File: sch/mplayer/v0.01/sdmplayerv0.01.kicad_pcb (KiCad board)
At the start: 2 copper layers, 47.2 x 69.6 mm, 73 parts, among them CON1 SD_Card, IC1 AT24CS64-SSHM, J1 JACK_TRS_6PINS, P1 USB_OTG, P2 CONN_01X09, P3 ClockBat, P4 USART1, P6 LiPo battery, SW1 SW_PUSH, SW2 Switch_SPDT_x2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

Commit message: Fixed traces
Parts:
- moved P2 19.0 mm to (187.3, 132.0)
- moved SW2 16.6 mm to (188.0, 112.3)
- moved C12 10.2 mm to (187.9, 108.3)
- moved C9 10.2 mm to (187.9, 106.0)
- moved L1 10.2 mm to (188.0, 101.7)
- moved U2 10.2 mm to (183.5, 104.0)
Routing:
- net +3V3: track 275.4 -> 321.4 mm
- net /I2C2_SDA: track 44.3 -> 16.0 mm
- net /I2C2_SCL: track 43.6 -> 15.6 mm
- net /PB2: track 42.5 -> 15.2 mm
- net /PB1: track 40.7 -> 14.8 mm
- net /PB0: track 40.2 -> 15.2 mm
- net Net-(P6-Pad2): track 7.08 -> 27.9 mm
- net /PC4: track 36.5 -> 16.0 mm
- net /PC5: track 35.9 -> 15.6 mm
- net +BATT: track 85.5 -> 104.1 mm
- net /SD_CONN: track 53.7 -> 41.5 mm
- net GND: track 537.5 -> 528.3 mm, vias 15 -> 18
- net /SD_CLK: track 53.8 -> 48.7 mm
- net /DAT3: track 55.1 -> 51.8 mm
- net /SD_CMD: track 53.3 -> 50.3 mm
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
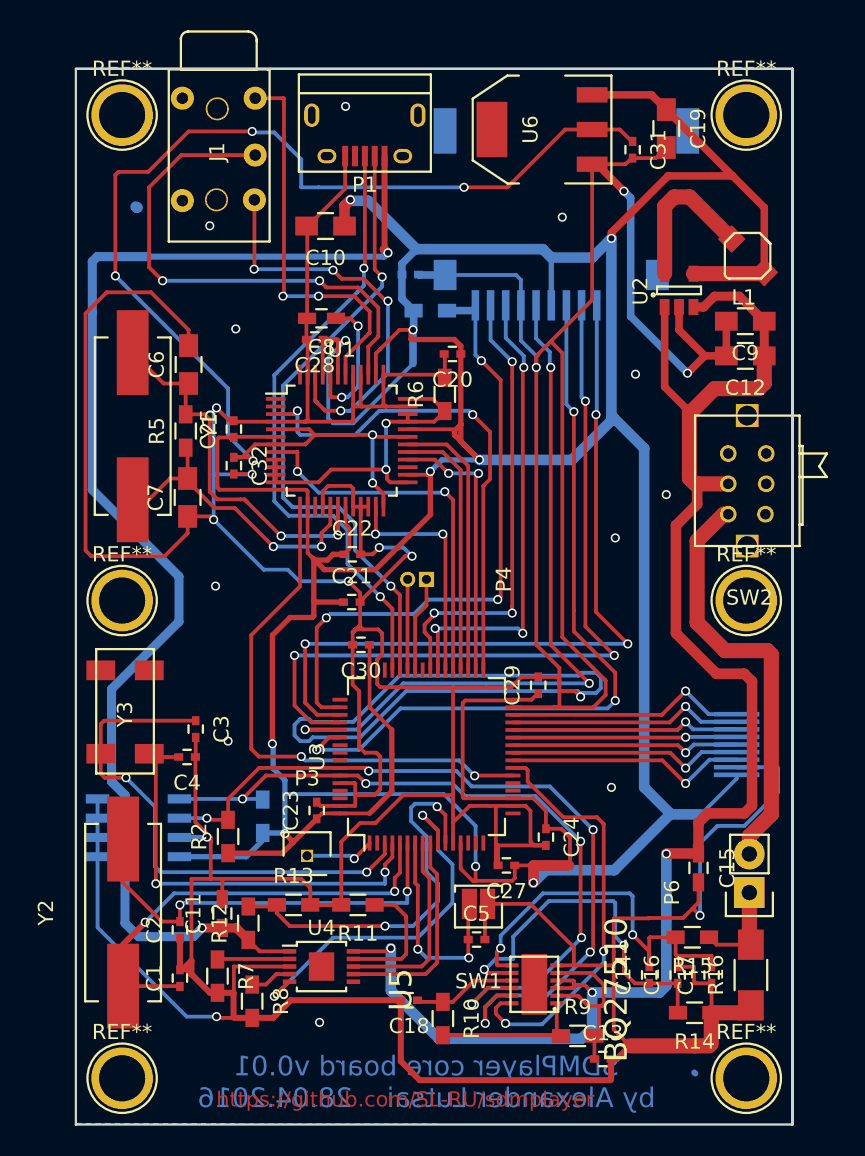
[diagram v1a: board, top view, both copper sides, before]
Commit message: SD footprint
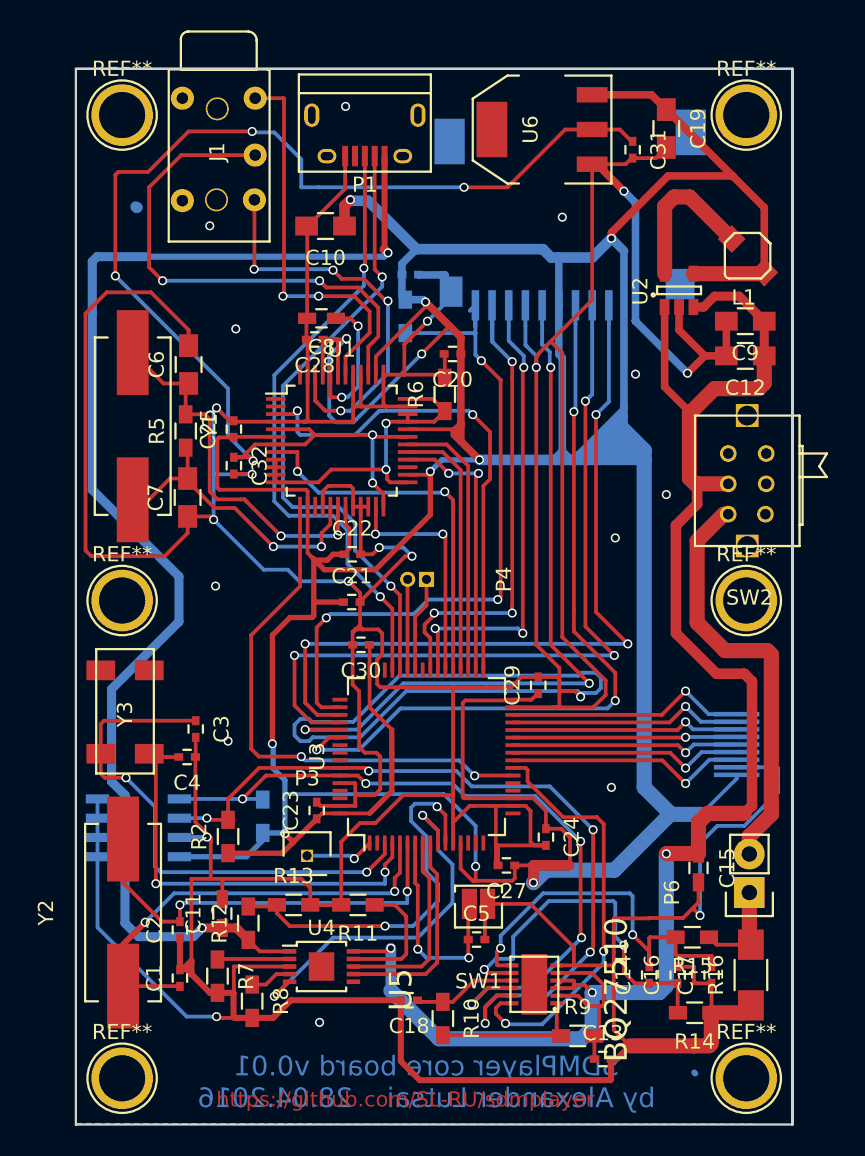
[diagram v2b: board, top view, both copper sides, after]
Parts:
- CON1: footprint v0:Micro_SD_card_slot -> Micro_SD_card_slot
- moved R3 1.69 mm to (165.5, 105.7), turned to 270 degrees
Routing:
- net +3V3: track 321.4 -> 375.2 mm, vias 10 -> 11
- net /SD_CONN: track 41.5 -> 46.6 mm
- net GND: track 528.3 -> 532.2 mm, vias 18 -> 14
- net /DAT1: track 30.2 -> 33.9 mm
- net /DAT3: track 51.8 -> 52.4 mm
- net (no net): vias 6 -> 11

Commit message: Final pcb
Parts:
- moved C12 31.4 mm to (181.5, 139.1)
- moved C10 27.6 mm to (187.8, 98.6)
- moved U2 5.03 mm to (187.8, 106.6)
- moved C9 3.22 mm to (184.7, 106.6), turned to 90 degrees
- moved L1 0.39 mm to (188.0, 102.1), turned to 90 degrees
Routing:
- net GND: track 532.2 -> 517.3 mm, vias 14 -> 18
- net Net-(L1-Pad1): track 10.3 -> 2.37 mm
- net /SD_CLK: track 48.7 -> 52.1 mm
- net +BATT: track 104.1 -> 100.8 mm
- net +3V3: track 375.2 -> 372.1 mm, vias 11 -> 10
- net /SD_CONN: track 46.6 -> 44.9 mm
- net /DAT0: track 30.8 -> 29.5 mm
- net /DAT2: track 51.3 -> 50.1 mm
- net /DAT1: track 33.9 -> 32.8 mm
- net /DAT3: track 52.4 -> 51.5 mm
- net (no net): track 0.24 -> 0.00 mm, vias 11 -> 1

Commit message: fix
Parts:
- added C33: 100pF, Capacitors_SMD:C_0805_HandSoldering, B.Cu at (149.9, 131.5)
- added P5: CONN_01X03, Socket_Strips:Socket_Strip_Straight_1x03, F.Cu at (152.7, 129.9)
- added P7: gnd, Socket_Strips:Socket_Strip_Straight_1x01, F.Cu at (182.6, 111.9)
- added P8: gnd, Socket_Strips:Socket_Strip_Straight_1x01, F.Cu at (151.0, 153.9)
- added P9: 3.3v, Socket_Strips:Socket_Strip_Straight_1x01, F.Cu at (182.4, 116.2)
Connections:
- U3 pad 46: Net-(U3-Pad46) -> /SWDIO
- U3 pad 49: Net-(U3-Pad49) -> /SWCLK
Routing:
- net (no net): track 0.00 -> 47.6 mm
- net /SWCLK: track 0.00 -> 19.9 mm, vias 0 -> 2
- net /SWDIO: track 0.00 -> 19.3 mm, vias 0 -> 2
- net GND: track 517.3 -> 529.7 mm
- net +3V3: track 372.1 -> 380.8 mm
